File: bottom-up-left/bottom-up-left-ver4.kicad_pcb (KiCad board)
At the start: 2 copper layers, 234.5 x 137.6 mm, 125 parts, among them U1 ProMicro, U2 PJ-320A

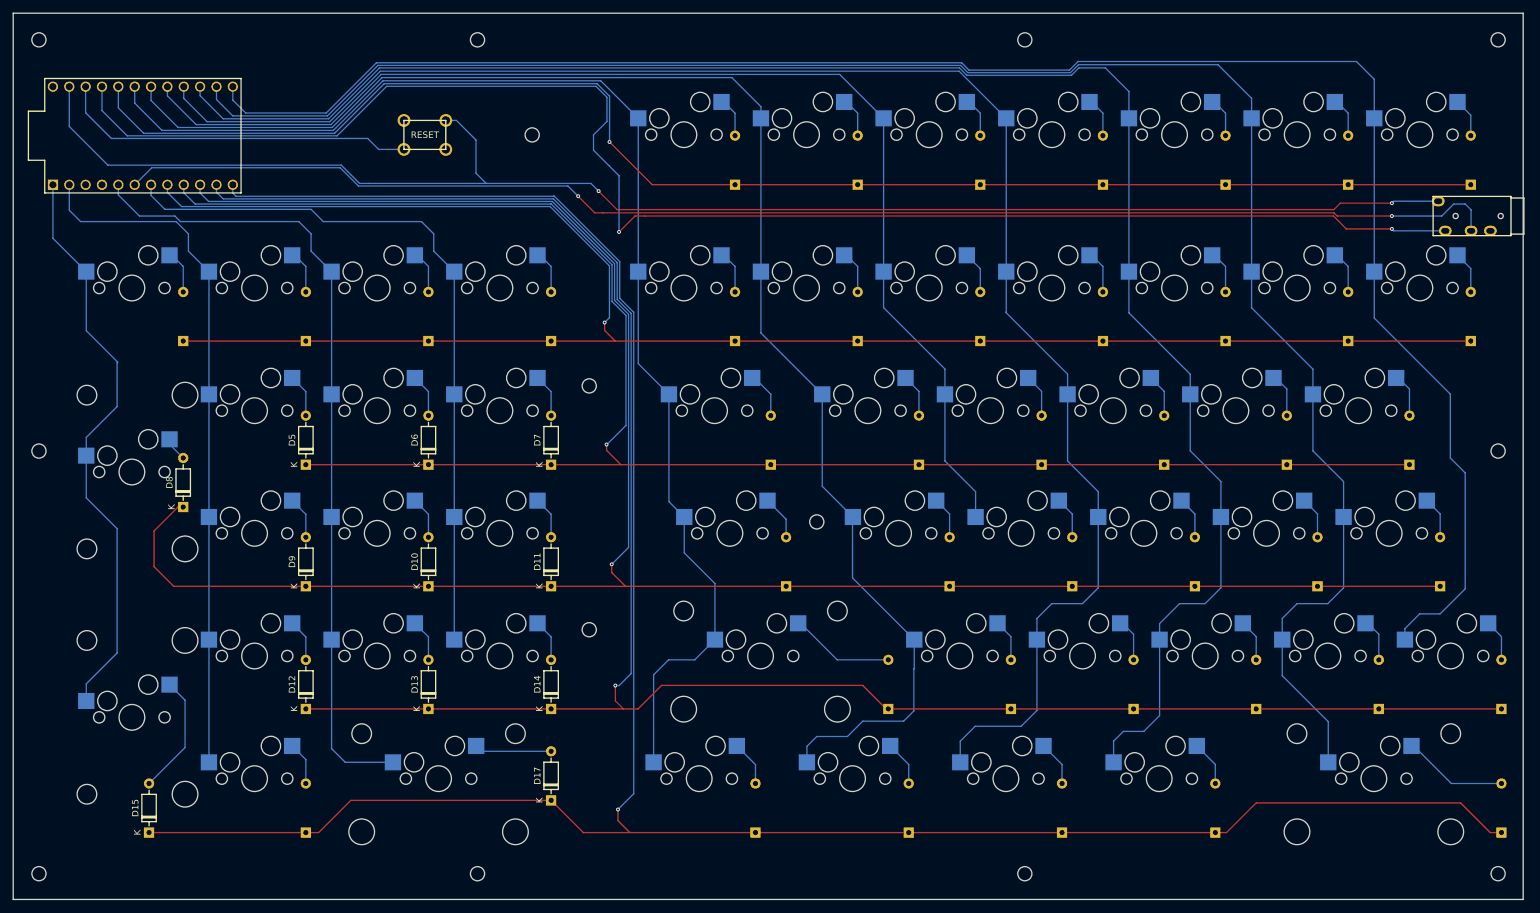
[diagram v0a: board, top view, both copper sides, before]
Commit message: Fix: relocated left PCB wire more tight
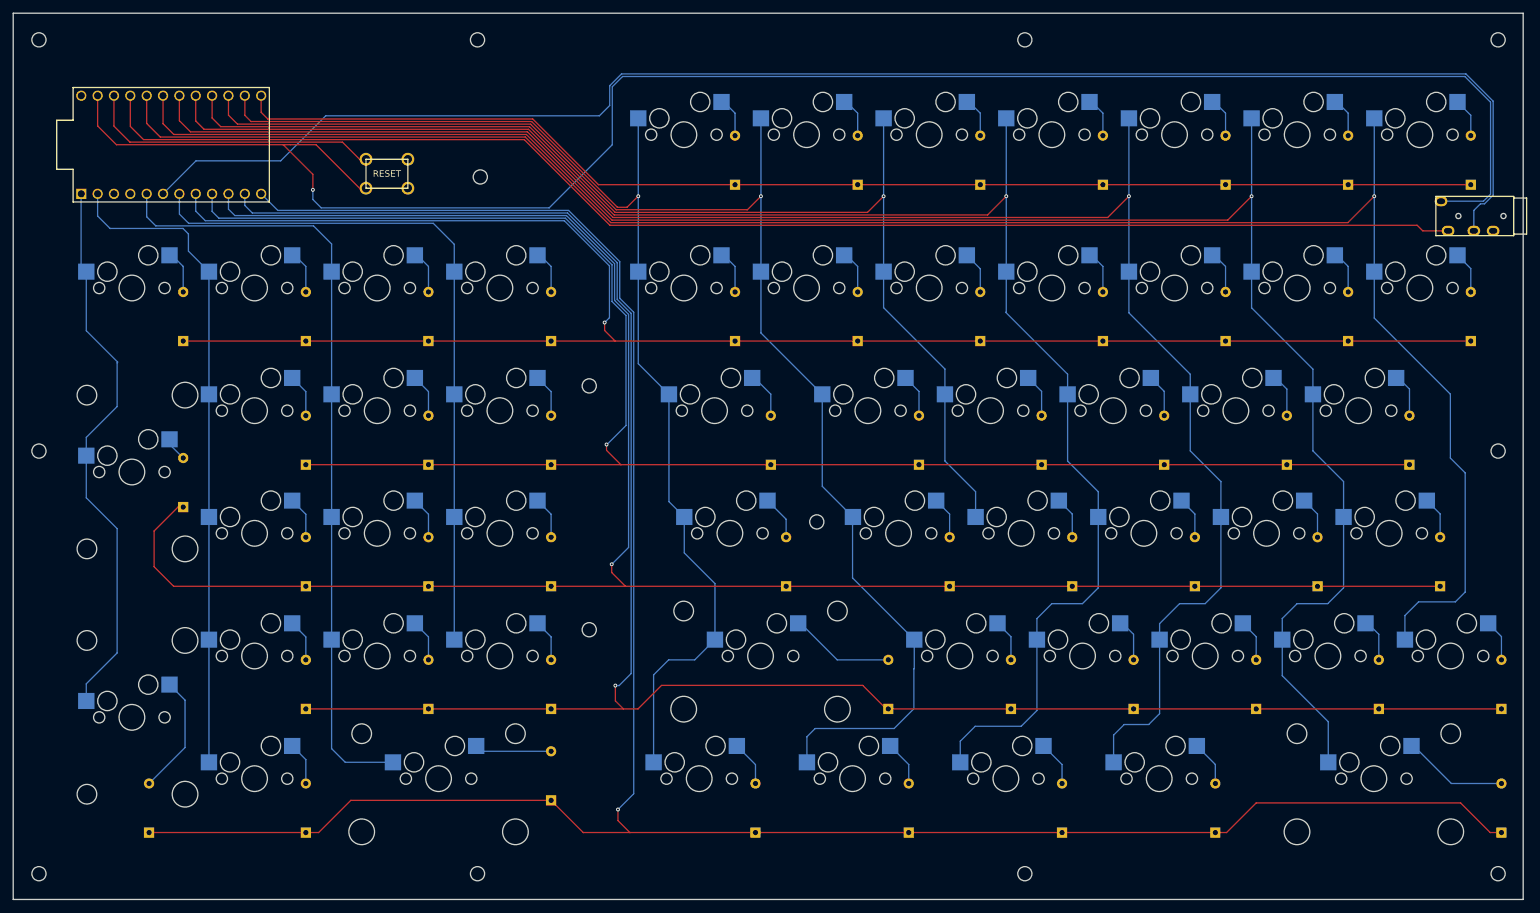
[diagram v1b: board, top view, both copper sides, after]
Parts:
- D10, D11, D12, D13, D14, D15, D17, D5, D6, D7, D8, D9: moved to B.Cu
- moved REF** 10.4 mm to (90.5, 44.5)
- moved RESET1 8.43 mm to (76.0, 44.0), turned to 0 degrees
- moved U1 4.62 mm to (42.5, 39.5)
- moved U2 0.43 mm to (251.0, 50.6)
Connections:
- U1 pad 13: col11 -> row1
- U1 pad 14: col10 -> col5
- U1 pad 15: col9 -> col6
- U1 pad 16: col8 -> col7
- U1 pad 17: col7 -> col8
- U1 pad 18: col6 -> col9
- U1 pad 19: col5 -> col10
- U1 pad 20: row1 -> col11
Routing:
- net GND: track 238.0 -> 281.7 mm, vias 2 -> 1
- net row1: track 228.8 -> 195.1 mm, vias 1 -> 0
- net VCC: track 241.4 -> 216.1 mm, vias 2 -> 0
- net SCL: track 216.1 -> 239.6 mm, vias 2 -> 0
- net col5: track 199.4 -> 182.0 mm, vias 0 -> 1
- net col11: track 284.2 -> 297.1 mm, vias 0 -> 1
- net col6: track 228.8 -> 216.7 mm, vias 0 -> 1
- net RESET: track 55.8 -> 45.7 mm
- net col10: track 288.9 -> 296.8 mm, vias 0 -> 1
- net row6: track 375.3 -> 369.4 mm
- net col7: track 188.4 -> 182.7 mm, vias 0 -> 1
- net col2: track 107.4 -> 102.1 mm
- net row5: track 328.7 -> 324.1 mm
- net row4: track 335.8 -> 331.4 mm
- net row3: track 278.0 -> 273.8 mm
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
